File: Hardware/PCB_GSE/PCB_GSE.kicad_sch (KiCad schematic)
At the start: 0 parts

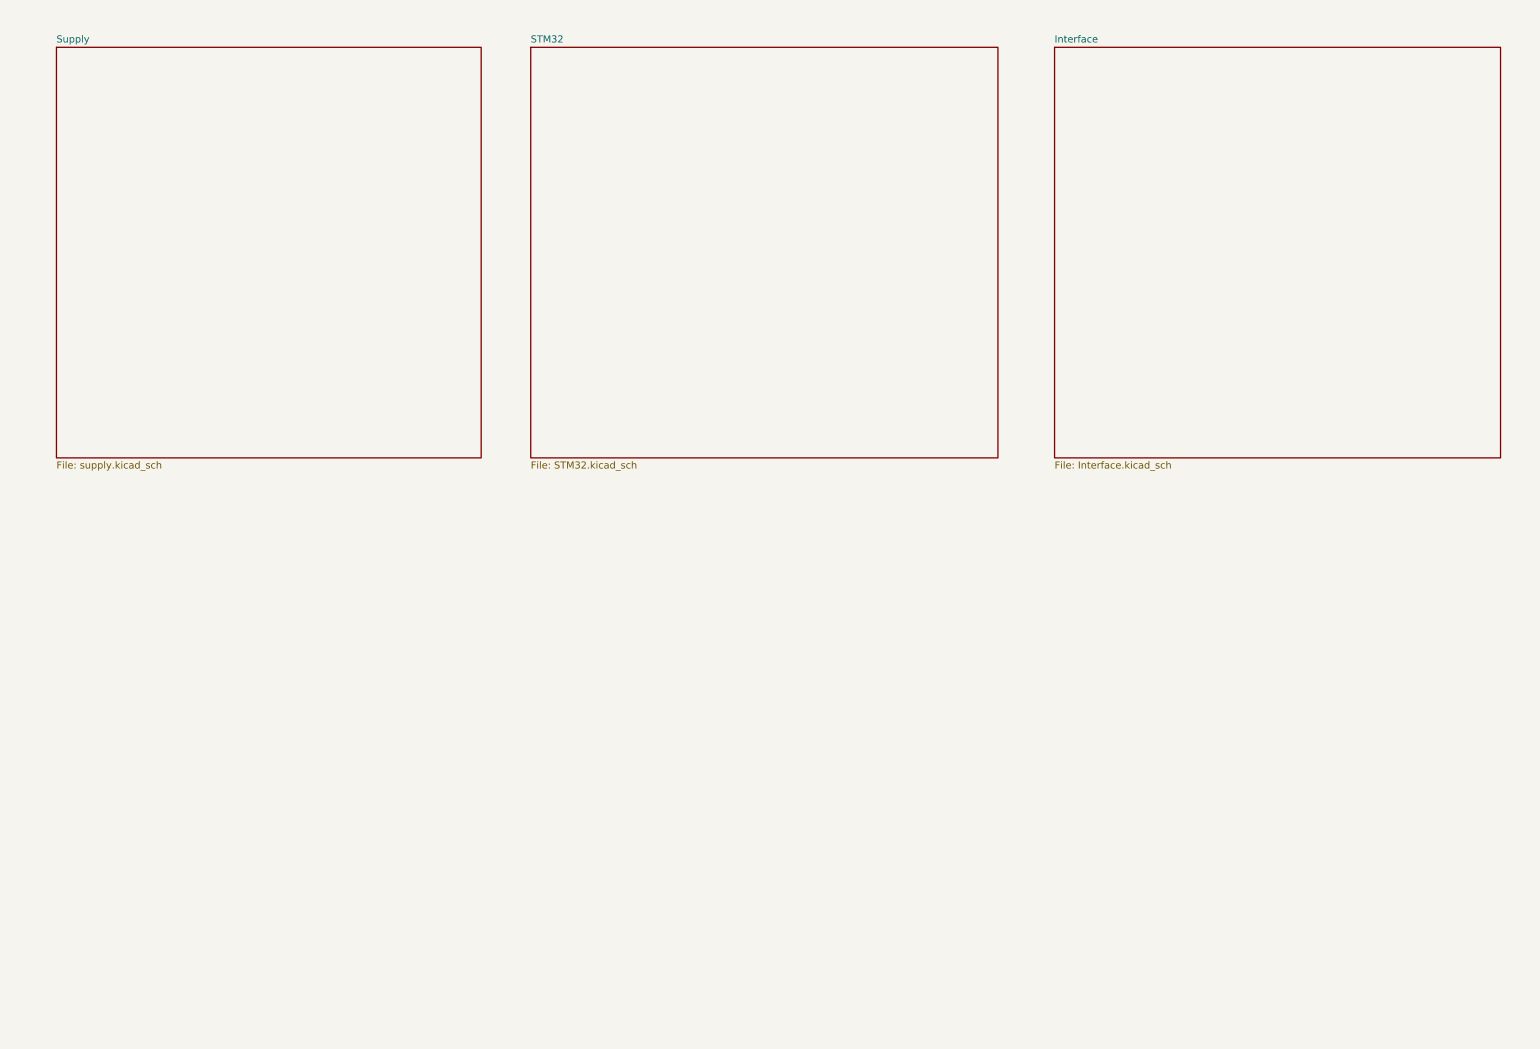
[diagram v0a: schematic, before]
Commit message: hierarchisation des feuille
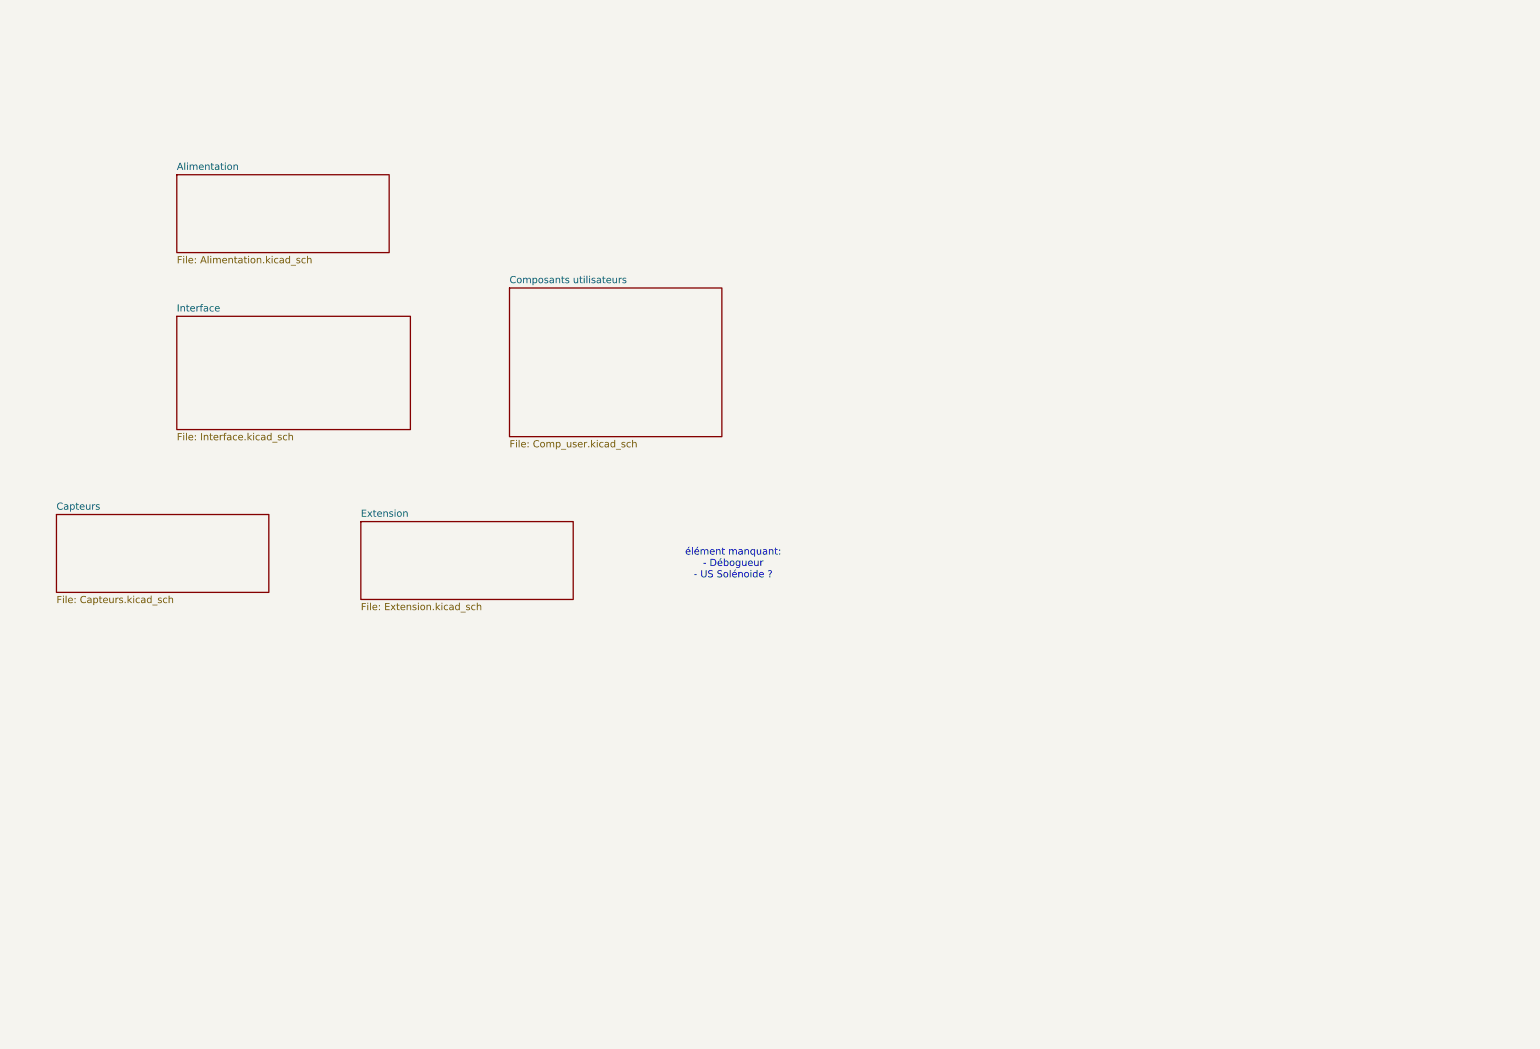
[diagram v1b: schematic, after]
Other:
- removed sheet STM32
- removed sheet Supply
- added sheet Alimentation (Alimentation.kicad_sch)
- added sheet Capteurs (Capteurs.kicad_sch)
- added sheet Composants utilisateurs (Comp_user.kicad_sch)
- added sheet Extension (Extension.kicad_sch)
- note added: "élément manquant: - Débogueur - US Solénoide ?"
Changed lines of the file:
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@@
 	(generator_version "9.0")
 	(paper "A4")
-	(sheet
-		(at 19.05 19.05)
-		(size 76.2 73.66)
-		(exclude_from_sim no)
-		(in_bom yes)
-		(on_board yes)
-		(dnp no)
-		(fields_autoplaced yes)
-		(stroke
-			(width 0.1524)
-			(type solid)
-		)
-		(fill
-			(color 0 0 0 0.0000)
-		)
-		(property "Sheetname" "Supply"
-			(at 19.05 18.3384 0)
-			(effects
-				(font
-					(size 1.27 1.27)
-				)
-				(justify left bottom)
-			)
-		)
-		(property "Sheetfile" "supply.kicad_sch"
-			(at 19.05 93.2946 0)
-			(effects
-				(font
-					(size 1.27 1.27)
-				)
-				(justify left top)
-			)
-		)
-		(instances
-			(project "PCB_GSE"
-				(path "/fb1e7f9a-1970-407a-9a24-5aea0f0ce853"
+	(text "élément manquant:\n- Débogueur\n- US Solénoide ?"
+		(exclude_from_sim no)
+		(at 140.462 111.76 0)
+		(effects
+			(font
+				(size 1.27 1.27)
+			)
+		)
+	)
+	(sheet
+		(at 40.64 41.91)
+		(size 38.1 13.97)
+		(exclude_from_sim no)
+		(in_bom yes)
+		(on_board yes)
+		(dnp no)
+		(fields_autoplaced yes)
+		(stroke
+			(width 0.1524)
+			(type solid)
+		)
+		(fill
+			(color 0 0 0 0.0000)
+		)
+		(property "Sheetname" "Alimentation"
+			(at 40.64 41.1984 0)
+			(effects
+				(font
+					(size 1.27 1.27)
+				)
+				(justify left bottom)
+			)
+		)
+		(property "Sheetfile" "Alimentation.kicad_sch"
+			(at 40.64 56.4646 0)
+			(effects
+				(font
+					(size 1.27 1.27)
+				)
+				(justify left top)
+			)
+		)
+		(instances
+			(project "PCB_GSE"
+				(path "/a63f9ed4-21e4-42d0-8bfc-f96143f84d4d"
 					(page "2")
 				)
@@
 	)
 	(sheet
-		(at 198.12 19.05)
-		(size 80.01 73.66)
+		(at 73.66 104.14)
+		(size 38.1 13.97)
+		(exclude_from_sim no)
+		(in_bom yes)
+		(on_board yes)
+		(dnp no)
+		(fields_autoplaced yes)
+		(stroke
+			(width 0.1524)
+			(type solid)
+		)
+		(fill
+			(color 0 0 0 0.0000)
+		)
+		(property "Sheetname" "Extension"
+			(at 73.66 103.4284 0)
+			(effects
+				(font
+					(size 1.27 1.27)
+				)
+				(justify left bottom)
+			)
+		)
+		(property "Sheetfile" "Extension.kicad_sch"
+			(at 73.66 118.6946 0)
+			(effects
+				(font
+					(size 1.27 1.27)
+				)
+				(justify left top)
+			)
+		)
+		(instances
+			(project "PCB_GSE"
+				(path "/a63f9ed4-21e4-42d0-8bfc-f96143f84d4d"
+					(page "5")
+				)
+			)
+		)
+	)
+	(sheet
+		(at 19.05 102.87)
+		(size 38.1 13.97)
+		(exclude_from_sim no)
+		(in_bom yes)
+		(on_board yes)
+		(dnp no)
+		(fields_autoplaced yes)
+		(stroke
+			(width 0.1524)
+			(type solid)
+		)
+		(fill
+			(color 0 0 0 0.0000)
+		)
+		(property "Sheetname" "Capteurs"
+			(at 19.05 102.1584 0)
+			(effects
+				(font
+					(size 1.27 1.27)
+				)
+				(justify left bottom)
+			)
+		)
+		(property "Sheetfile" "Capteurs.kicad_sch"
+			(at 19.05 117.4246 0)
+			(effects
+				(font
+					(size 1.27 1.27)
+				)
+				(justify left top)
+			)
+		)
+		(instances
+			(project "PCB_GSE"
+				(path "/a63f9ed4-21e4-42d0-8bfc-f96143f84d4d"
+					(page "3")
+				)
+			)
+		)
+	)
+	(sheet
+		(at 100.33 62.23)
+		(size 38.1 26.67)
+		(exclude_from_sim no)
+		(in_bom yes)
+		(on_board yes)
+		(dnp no)
+		(fields_autoplaced yes)
+		(stroke
+			(width 0.1524)
+			(type solid)
+		)
+		(fill
+			(color 0 0 0 0.0000)
+		)
+		(property "Sheetname" "Composants utilisateurs"
+			(at 100.33 61.5184 0)
+			(effects
+				(font
+					(size 1.27 1.27)
+				)
+				(justify left bottom)
+			)
+		)
+		(property "Sheetfile" "Comp_user.kicad_sch"
+			(at 100.33 89.4846 0)
+			(effects
+				(font
+					(size 1.27 1.27)
+				)
+				(justify left top)
+			)
+		)
+		(instances
+			(project "PCB_GSE"
+				(path "/a63f9ed4-21e4-42d0-8bfc-f96143f84d4d"
+					(page "4")
+				)
+			)
+		)
+	)
+	(sheet
+		(at 40.64 67.31)
+		(size 41.91 20.32)
 		(exclude_from_sim no)
 		(in_bom yes)
@@
 		)
 		(property "Sheetname" "Interface"
-			(at 198.12 18.3384 0)
+			(at 40.64 66.5984 0)
 			(effects
 				(font
@@
 		)
 		(property "Sheetfile" "Interface.kicad_sch"
-			(at 198.12 93.2946 0)
-			(effects
-				(font
-					(size 1.27 1.27)
-				)
-				(justify left top)
-			)
-		)
-		(instances
-			(project "PCB_GSE"
-				(path "/fb1e7f9a-1970-407a-9a24-5aea0f0ce853"
-					(page "4")
-				)
-			)
-		)
-	)
-	(sheet
-		(at 104.14 19.05)
-		(size 83.82 73.66)
-		(exclude_from_sim no)
-		(in_bom yes)
-		(on_board yes)
-		(dnp no)
-		(fields_autoplaced yes)
-		(stroke
-			(width 0.1524)
-			(type solid)
-		)
-		(fill
-			(color 0 0 0 0.0000)
-		)
-		(property "Sheetname" "STM32"
-			(at 104.14 18.3384 0)
-			(effects
-				(font
-					(size 1.27 1.27)
-				)
-				(justify left bottom)
-			)
-		)
-		(property "Sheetfile" "STM32.kicad_sch"
-			(at 104.14 93.2946 0)
-			(effects
-				(font
-					(size 1.27 1.27)
-				)
-				(justify left top)
-			)
-		)
-		(instances
-			(project "PCB_GSE"
-				(path "/fb1e7f9a-1970-407a-9a24-5aea0f0ce853"
-					(page "3")
-				)
-			)
+			(at 40.64 88.2146 0)
+			(effects
+				(font
+					(size 1.27 1.27)
+				)
+				(justify left top)
+			)
+		)
+		(instances
+			(project "PCB_GSE"
+				(path "/a63f9ed4-21e4-42d0-8bfc-f96143f84d4d"
+					(page "6")
+				)
+			)

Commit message: un peux d'avancement (brouillon)
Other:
- sheet Capteurs renamed Capteur
- sheet Interface renamed STM32
- sheet Capteur ports: added 3V3, LCell_An, LCell_sleep, P_An, P_sleep, Temp_An, Vin; removed none
- sheet Composants utilisateurs ports: added 3V3, ISO_CAN_IN, ISO_CAN_RXD, ISO_CAN_TXD; removed none
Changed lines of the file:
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@@
 	(text "élément manquant:\n- Débogueur\n- US Solénoide ?"
 		(exclude_from_sim no)
-		(at 140.462 111.76 0)
+		(at 160.782 114.3 0)
 		(effects
 			(font
@@
 	)
 	(sheet
-		(at 73.66 104.14)
+		(at 93.98 106.68)
 		(size 38.1 13.97)
 		(exclude_from_sim no)
@@
 		)
 		(property "Sheetname" "Extension"
-			(at 73.66 103.4284 0)
+			(at 93.98 105.9684 0)
 			(effects
 				(font
@@
 		)
 		(property "Sheetfile" "Extension.kicad_sch"
-			(at 73.66 118.6946 0)
+			(at 93.98 121.2346 0)
 			(effects
 				(font
@@
 	)
 	(sheet
-		(at 19.05 102.87)
-		(size 38.1 13.97)
-		(exclude_from_sim no)
-		(in_bom yes)
-		(on_board yes)
-		(dnp no)
-		(fields_autoplaced yes)
-		(stroke
-			(width 0.1524)
-			(type solid)
-		)
-		(fill
-			(color 0 0 0 0.0000)
-		)
-		(property "Sheetname" "Capteurs"
-			(at 19.05 102.1584 0)
+		(at 39.37 105.41)
+		(size 38.1 17.78)
+		(exclude_from_sim no)
+		(in_bom yes)
+		(on_board yes)
+		(dnp no)
+		(fields_autoplaced yes)
+		(stroke
+			(width 0.1524)
+			(type solid)
+		)
+		(fill
+			(color 0 0 0 0.0000)
+		)
+		(property "Sheetname" "Capteur"
+			(at 39.37 104.6984 0)
 			(effects
 				(font
@@
 		)
 		(property "Sheetfile" "Capteurs.kicad_sch"
-			(at 19.05 117.4246 0)
-			(effects
-				(font
-					(size 1.27 1.27)
-				)
-				(justify left top)
+			(at 39.37 123.7746 0)
+			(effects
+				(font
+					(size 1.27 1.27)
+				)
+				(justify left top)
+			)
+		)
+		(pin "LCell_An" output
+			(at 77.47 110.49 0)
+			(effects
+				(font
+					(size 1.27 1.27)
+				)
+				(justify right)
+			)
+		)
+		(pin "LCell_sleep" input
+			(at 77.47 113.03 0)
+			(effects
+				(font
+					(size 1.27 1.27)
+				)
+				(justify right)
+			)
+		)
+		(pin "P_An" output
+			(at 77.47 118.11 0)
+			(effects
+				(font
+					(size 1.27 1.27)
+				)
+				(justify right)
+			)
+		)
+		(pin "P_sleep" input
+			(at 77.47 120.65 0)
+			(effects
+				(font
+					(size 1.27 1.27)
+				)
+				(justify right)
+			)
+		)
+		(pin "Temp_An" output
+			(at 77.47 107.95 0)
+			(effects
+				(font
+					(size 1.27 1.27)
+				)
+				(justify right)
+			)
+		)
+		(pin "Vin" input
+			(at 39.37 110.49 180)
+			(effects
+				(font
+					(size 1.27 1.27)
+				)
+				(justify left)
+			)
+		)
+		(pin "3V3" input
+			(at 39.37 107.95 180)
+			(effects
+				(font
+					(size 1.27 1.27)
+				)
+				(justify left)
 			)
 		)
@@
 	(sheet
 		(at 100.33 62.23)
-		(size 38.1 26.67)
+		(size 29.21 26.67)
 		(exclude_from_sim no)
 		(in_bom yes)
@@
 			)
 		)
+		(pin "ISO_CAN_IN" input
+			(at 100.33 66.04 180)
+			(effects
+				(font
+					(size 1.27 1.27)
+				)
+				(justify left)
+			)
+		)
+		(pin "ISO_CAN_RXD" output
+			(at 100.33 68.58 180)
+			(effects
+				(font
+					(size 1.27 1.27)
+				)
+				(justify left)
+			)
+		)
+		(pin "ISO_CAN_TXD" input
+			(at 100.33 71.12 180)
+			(effects
+				(font
+					(size 1.27 1.27)
+				)
+				(justify left)
+			)
+		)
+		(pin "3V3" input
+			(at 129.54 66.04 0)
+			(effects
+				(font
+					(size 1.27 1.27)
+				)
+				(justify right)
+			)
+		)
 		(instances
 			(project "PCB_GSE"
@@
 			(color 0 0 0 0.0000)
 		)
-		(property "Sheetname" "Interface"
+		(property "Sheetname" "STM32"
 			(at 40.64 66.5984 0)
 			(effects
